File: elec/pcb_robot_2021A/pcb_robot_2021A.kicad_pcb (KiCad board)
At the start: 2 copper layers, 99 x 79 mm, 43 parts, among them J1 LCD, J10 Encodeur 1, J11 Encodeur 2, J12 Conn_bat_pwr, J13 Tirette, J14 Couleur, J15 UART_backup, J16 Xbee, J17 PCA9685, J18 Capt_US, J19 I2C_backup, J2 IR 1.1, J20 lidar_in, J21 lidar_out, J22 Lidar_alim, J23 Galet 1.1, J24 Galet 1.2, J25 Galet 2.1, J26 Galet 2.2, J3 IR 1.2, J4 IR 1.3, J5 IR 2.1, J6 IR 2.2, J7 IR 2.3, J8 Moteur 1, J9 Moteur 2, U1 R-78E5.0-1.0, U2 Teensy3.5, U3 mosfet_lid_I1, U4 mosfet_lid_I2, U5 mosfet_lid_I3, U6 mosfet_lid_I4, U7 mosfet_lid_I5

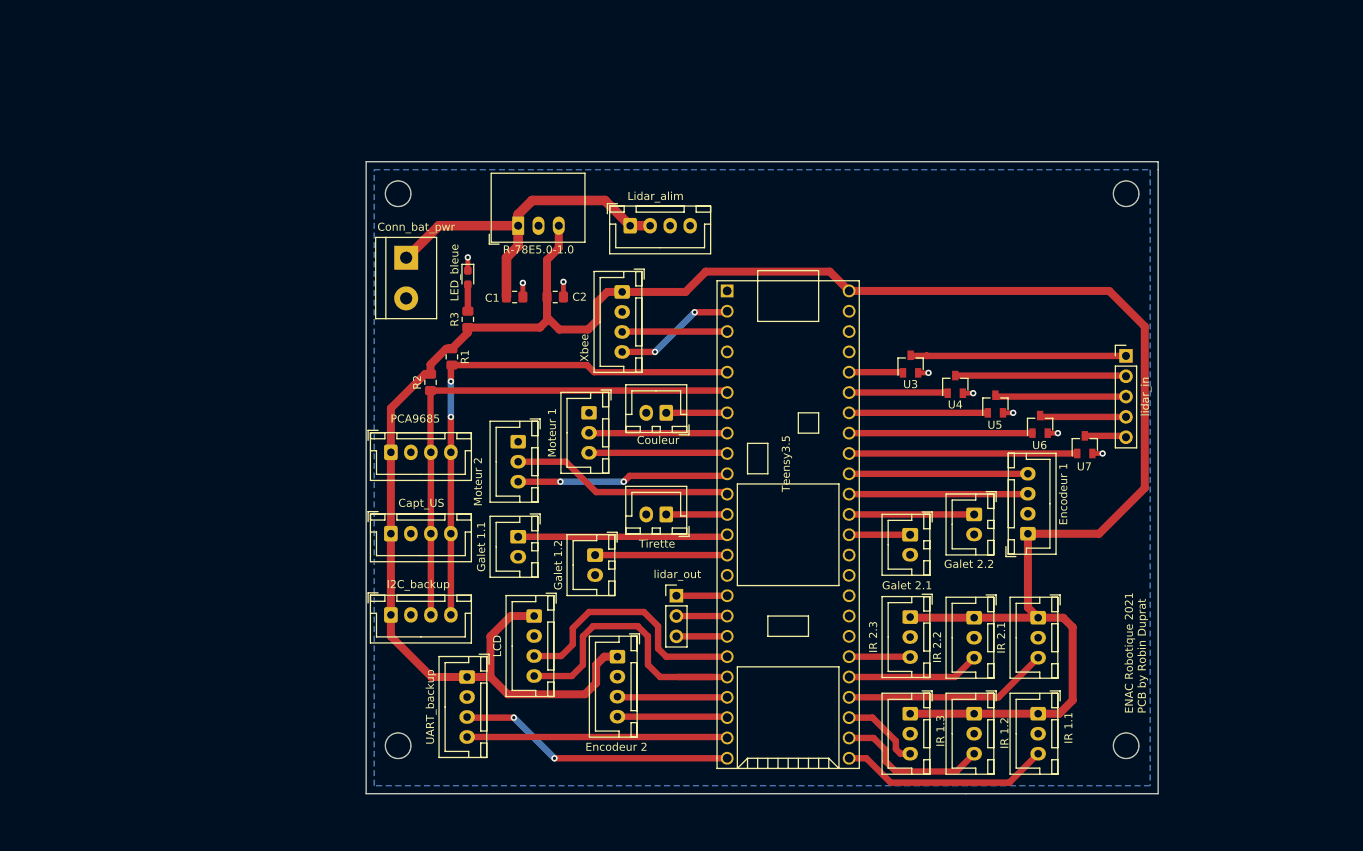
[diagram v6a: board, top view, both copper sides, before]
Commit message: Tentative de logo ENAC : echec Mise à jour visuelle, finission des cadres et plan de masse
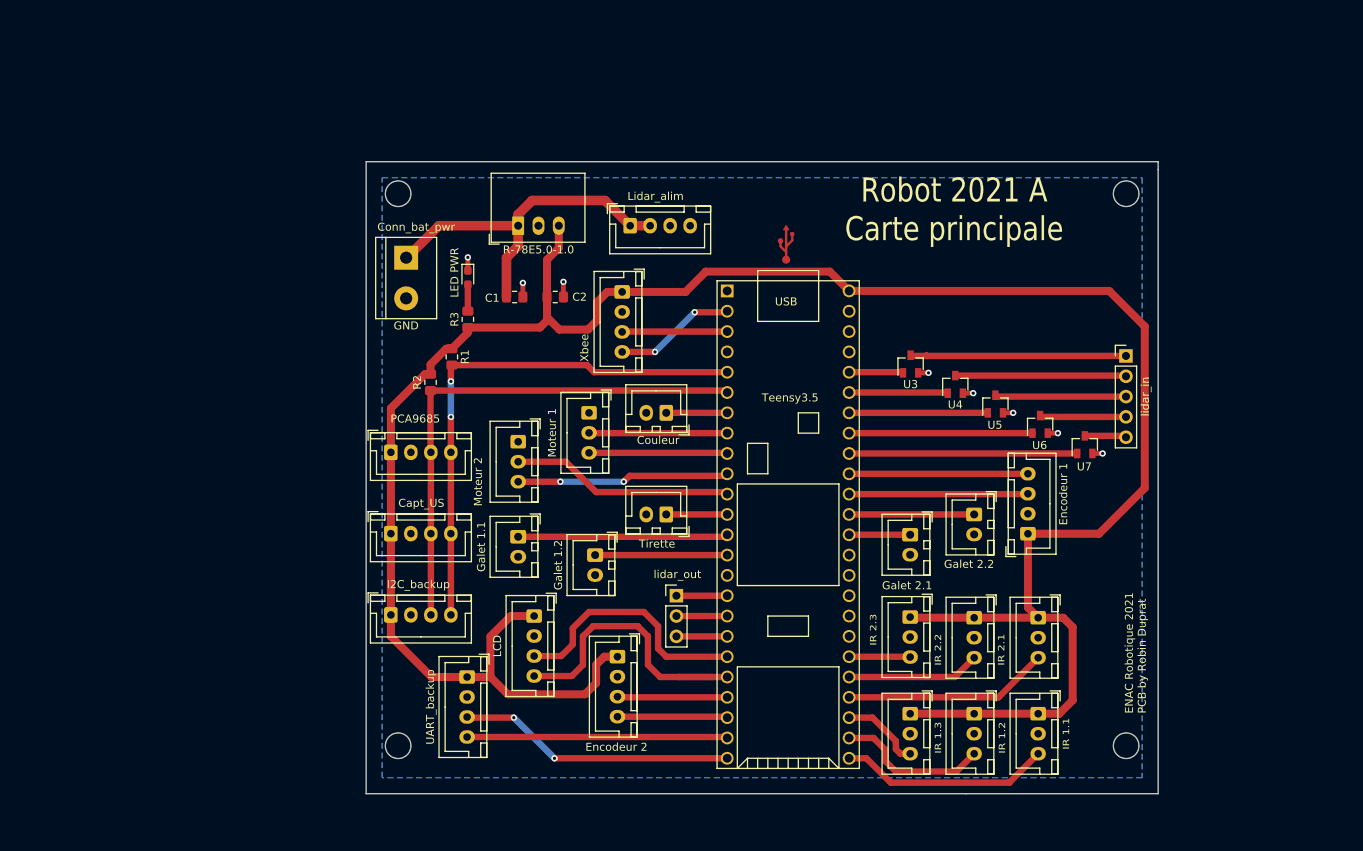
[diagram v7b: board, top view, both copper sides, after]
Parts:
- added REF**: USB_LOGO, myFootprints:USB_LOGO, F.Cu at (158.5, 53.2)
- D1: value LED_bleue -> LED PWR
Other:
- board text added: "GND"
- board text added: "USB"

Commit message: Patch footprint connecteurs servo sur carte PAC9685
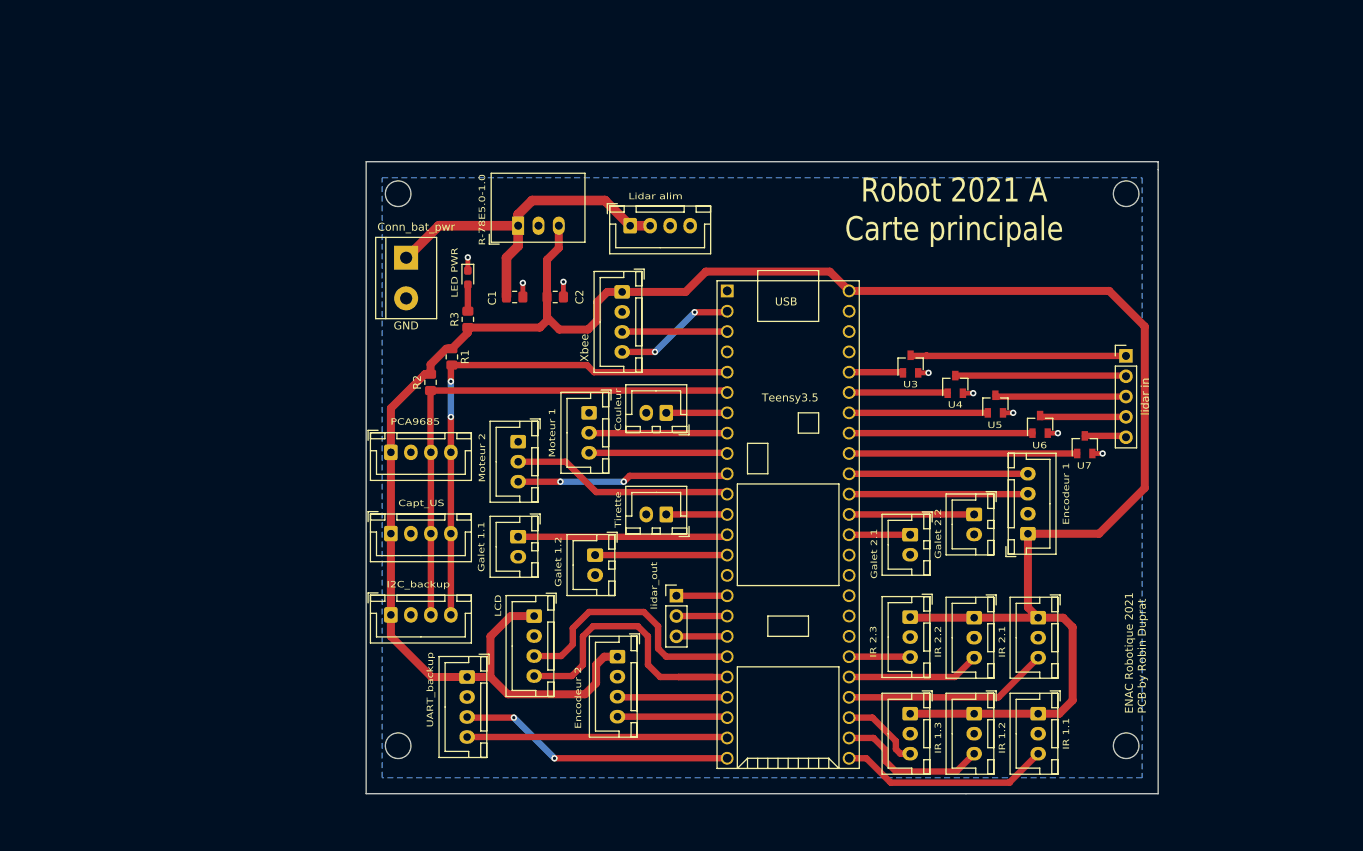
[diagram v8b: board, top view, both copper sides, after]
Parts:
- removed the REF** at (158.5, 53.2)
- J20: value lidar_in -> lidar in
- J22: value Lidar_alim -> Lidar alim
